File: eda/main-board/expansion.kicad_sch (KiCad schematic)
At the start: 15 parts, among them J2 Expansion, U11 74HCT245, U13 74HCT138, U17 74HCT541, U18 74HCT541, U20 74HCT541

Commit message: Did stuff
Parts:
- renumbered J2 to J7
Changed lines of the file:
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@@
 (kicad_sch
-	(version 20231120)
+	(version 20250114)
 	(generator "eeschema")
-	(generator_version "8.0")
+	(generator_version "9.0")
 	(paper "A4")
 	(junction
@@
 	(label "A2"
 		(at 73.66 50.8 0)
-		(fields_autoplaced yes)
 		(effects
 			(font
@@
 	(label "e{slash}~{IRQ}"
 		(at 120.65 138.43 0)
-		(fields_autoplaced yes)
 		(effects
 			(font
@@
 	(label "IoSelect4"
 		(at 146.05 76.2 0)
-		(fields_autoplaced yes)
 		(effects
 			(font
@@
 	(label "A3"
 		(at 73.66 53.34 0)
-		(fields_autoplaced yes)
 		(effects
 			(font
@@
 	(label "IoSelect5"
 		(at 146.05 78.74 0)
-		(fields_autoplaced yes)
 		(effects
 			(font
@@
 	(label "e{slash}~{IRQ}"
 		(at 200.66 93.98 0)
-		(fields_autoplaced yes)
 		(effects
 			(font
@@
 	(label "IoSelect2"
 		(at 101.6 163.83 0)
-		(fields_autoplaced yes)
 		(effects
 			(font
@@
 	(label "IoSelect1"
 		(at 101.6 161.29 0)
-		(fields_autoplaced yes)
 		(effects
 			(font
@@
 	(label "A15"
 		(at 72.39 118.11 0)
-		(fields_autoplaced yes)
 		(effects
 			(font
@@
 	(label "IoSelect6"
 		(at 146.05 81.28 0)
-		(fields_autoplaced yes)
 		(effects
 			(font
@@
 	(label "e{slash}~{NMI}"
 		(at 200.66 91.44 0)
-		(fields_autoplaced yes)
 		(effects
 			(font
@@
 	(label "A14"
 		(at 72.39 115.57 0)
-		(fields_autoplaced yes)
 		(effects
 			(font
@@
 	(label "IoSelect2"
 		(at 146.05 71.12 0)
-		(fields_autoplaced yes)
 		(effects
 			(font
@@
 	(label "IoSelect7"
 		(at 101.6 176.53 0)
-		(fields_autoplaced yes)
 		(effects
 			(font
@@
 	(label "D2"
 		(at 195.58 48.26 0)
-		(fields_autoplaced yes)
 		(effects
 			(font
@@
 	(label "A13"
 		(at 72.39 113.03 0)
-		(fields_autoplaced yes)
 		(effects
 			(font
@@
 	(label "A10"
 		(at 72.39 105.41 0)
-		(fields_autoplaced yes)
 		(effects
 			(font
@@
 	(label "A7"
 		(at 74.93 161.29 0)
-		(fields_autoplaced yes)
 		(effects
 			(font
@@
 	(label "A9"
 		(at 72.39 102.87 0)
-		(fields_autoplaced yes)
 		(effects
 			(font
@@
 	(label "D6"
 		(at 195.58 58.42 0)
-		(fields_autoplaced yes)
 		(effects
 			(font
@@
 	(label "D7"
 		(at 195.58 60.96 0)
-		(fields_autoplaced yes)
 		(effects
 			(font
@@
 	(label "D0"
 		(at 195.58 43.18 0)
-		(fields_autoplaced yes)
 		(effects
 			(font
@@
 	(label "IoSelect1"
 		(at 146.05 68.58 0)
-		(fields_autoplaced yes)
 		(effects
 			(font
@@
 	(label "IoSelect6"
 		(at 101.6 173.99 0)
-		(fields_autoplaced yes)
 		(effects
 			(font
@@
 	(label "IoSelect0"
 		(at 146.05 66.04 0)
-		(fields_autoplaced yes)
 		(effects
 			(font
@@
 	(label "IoSelect5"
 		(at 101.6 171.45 0)
-		(fields_autoplaced yes)
 		(effects
 			(font
@@
 	(label "IoSelect7"
 		(at 146.05 83.82 0)
-		(fields_autoplaced yes)
 		(effects
 			(font
@@
 	(label "A8"
 		(at 74.93 163.83 0)
-		(fields_autoplaced yes)
 		(effects
 			(font
@@
 	(label "IoSelect0"
 		(at 101.6 158.75 0)
-		(fields_autoplaced yes)
 		(effects
 			(font
@@
 	(label "A6"
 		(at 74.93 158.75 0)
-		(fields_autoplaced yes)
 		(effects
 			(font
@@
 	(label "A11"
 		(at 72.39 107.95 0)
-		(fields_autoplaced yes)
 		(effects
 			(font
@@
 	(label "e{slash}~{NMI}"
 		(at 120.65 135.89 0)
-		(fields_autoplaced yes)
 		(effects
 			(font
@@
 	(label "D1"
 		(at 195.58 45.72 0)
-		(fields_autoplaced yes)
 		(effects
 			(font
@@
 	(label "A5"
 		(at 73.66 58.42 0)
-		(fields_autoplaced yes)
 		(effects
 			(font
@@
 	(label "D4"
 		(at 195.58 53.34 0)
-		(fields_autoplaced yes)
 		(effects
 			(font
@@
 	(label "IoSelect3"
 		(at 101.6 166.37 0)
-		(fields_autoplaced yes)
 		(effects
 			(font
@@
 	(label "A8"
 		(at 72.39 100.33 0)
-		(fields_autoplaced yes)
 		(effects
 			(font
@@
 	(label "IoSelect4"
 		(at 101.6 168.91 0)
-		(fields_autoplaced yes)
 		(effects
 			(font
@@
 	(label "IoSelect3"
 		(at 146.05 73.66 0)
-		(fields_autoplaced yes)
 		(effects
 			(font
@@
 	(label "A1"
 		(at 73.66 48.26 0)
-		(fields_autoplaced yes)
 		(effects
 			(font
@@
 	(label "A0"
 		(at 73.66 45.72 0)
-		(fields_autoplaced yes)
 		(effects
 			(font
@@
 	(label "A4"
 		(at 73.66 55.88 0)
-		(fields_autoplaced yes)
 		(effects
 			(font
@@
 	(label "A6"
 		(at 73.66 60.96 0)
-		(fields_autoplaced yes)
 		(effects
 			(font
@@
 	(label "~{ExtRomCS}"
 		(at 146.05 99.06 0)
-		(fields_autoplaced yes)
 		(effects
 			(font
@@
 	(label "A7"
 		(at 73.66 63.5 0)
-		(fields_autoplaced yes)
 		(effects
 			(font
@@
 	(label "A12"
 		(at 72.39 110.49 0)
-		(fields_autoplaced yes)
 		(effects
 			(font
@@
 	(label "D5"
 		(at 195.58 55.88 0)
-		(fields_autoplaced yes)
 		(effects
 			(font
@@
 	(label "D3"
 		(at 195.58 50.8 0)
-		(fields_autoplaced yes)
 		(effects
 			(font
@@
 		(shape bidirectional)
 		(at 168.91 137.16 0)
-		(fields_autoplaced yes)
 		(effects
 			(font
@@
 		(shape input)
 		(at 66.04 176.53 180)
-		(fields_autoplaced yes)
 		(effects
 			(font
@@
 		(shape bidirectional)
 		(at 168.91 134.62 0)
-		(fields_autoplaced yes)
 		(effects
 			(font
@@
 		(shape input)
 		(at 52.07 33.02 180)
-		(fields_autoplaced yes)
 		(effects
 			(font
@@
 		(shape output)
 		(at 163.83 127 0)
-		(fields_autoplaced yes)
 		(effects
 			(font
@@
 		(shape input)
 		(at 151.13 88.9 0)
-		(fields_autoplaced yes)
 		(effects
 			(font
@@
 		(shape input)
 		(at 220.98 35.56 0)
-		(fields_autoplaced yes)
 		(effects
 			(font
@@
 		(shape input)
 		(at 64.77 153.67 180)
-		(fields_autoplaced yes)
 		(effects
 			(font
@@
 		(shape input)
 		(at 165.1 66.04 180)
-		(fields_autoplaced yes)
 		(effects
 			(font
@@
 		(shape input)
 		(at 130.81 129.54 180)
-		(fields_autoplaced yes)
 		(effects
 			(font
@@
 		(dnp no)
 		(fields_autoplaced yes)
-		(property "Reference" "J2"
+		(property "Reference" "J7"
 			(at 139.7 35.56 0)
 			(effects

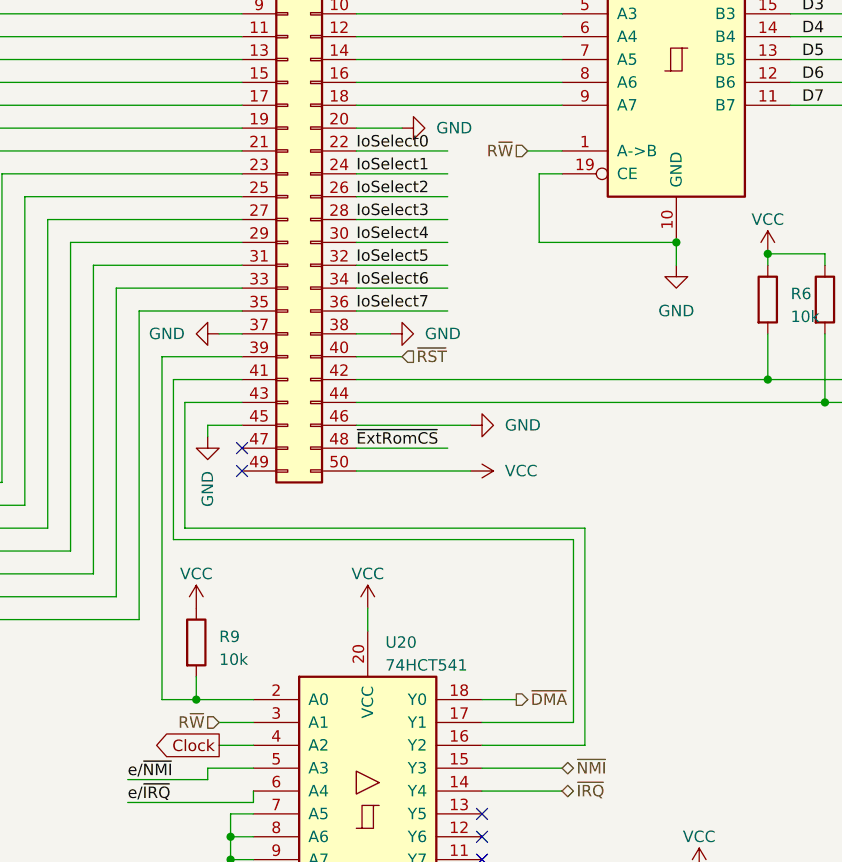
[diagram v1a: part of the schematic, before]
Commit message: fix: Traces straight over GND....
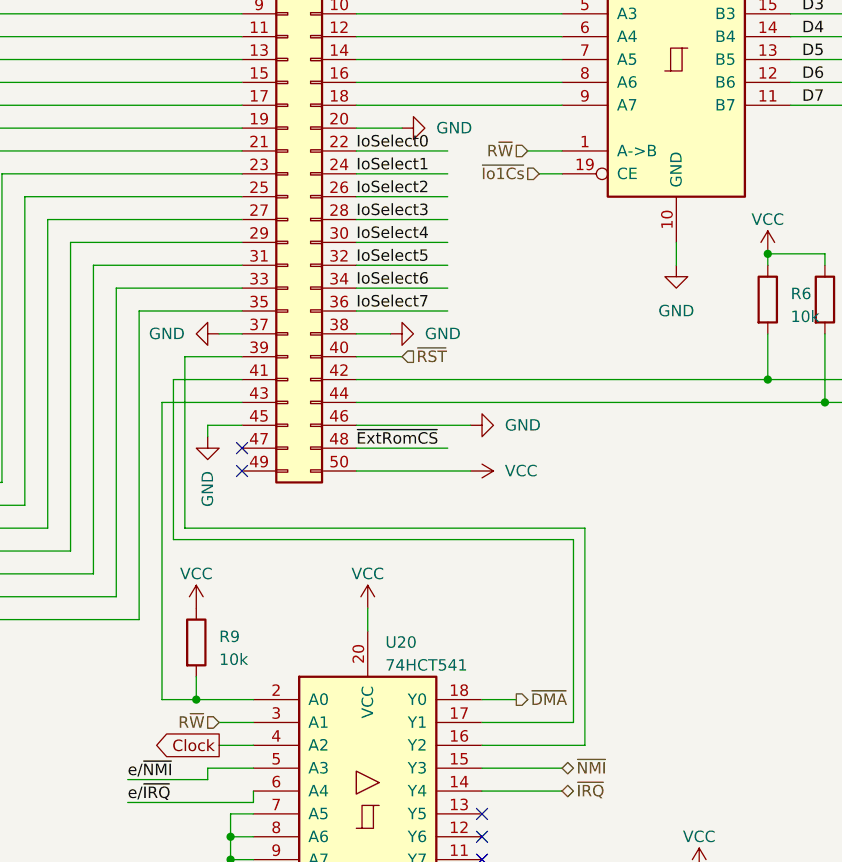
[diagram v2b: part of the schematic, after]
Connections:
- net GND: no longer U11.19 (CE)
- net ~{Io1Cs}: now also U11.19 (CE)
- net at R9.2, U20.2 (A0): now also J7.43 (Pin_43); no longer J7.39 (Pin_39)
- net at U20.16 (Y2): now also J7.39 (Pin_39); no longer J7.43 (Pin_43)
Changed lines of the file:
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@@
-	)
-	(junction
-		(at 181.61 76.2)
-		(diameter 0)
-		(color 0 0 0 0)
 	)
 	(junction
@@
 	(wire
 		(pts
+			(xy 124.46 93.98) (xy 133.35 93.98)
+		)
+		(stroke
+			(width 0)
+			(type default)
+		)
+	)
+	(wire
+		(pts
 			(xy 101.6 60.96) (xy 133.35 60.96)
 		)
@@
 	(wire
 		(pts
-			(xy 166.37 68.58) (xy 166.37 76.2)
-		)
-		(stroke
-			(width 0)
-			(type default)
-		)
-	)
-	(wire
-		(pts
 			(xy 111.76 73.66) (xy 111.76 107.95)
 		)
@@
 	(wire
 		(pts
-			(xy 127 107.95) (xy 127 93.98)
+			(xy 127 88.9) (xy 127 107.95)
 		)
 		(stroke
@@
 		)
 	)
-	(wire
-		(pts
-			(xy 127 93.98) (xy 133.35 93.98)
-		)
-		(stroke
-			(width 0)
-			(type default)
-		)
-	)
 	(bus
 		(pts
@@
 		)
 	)
+	(wire
+		(pts
+			(xy 127 88.9) (xy 133.35 88.9)
+		)
+		(stroke
+			(width 0)
+			(type default)
+		)
+	)
 	(bus
 		(pts
@@
 	(wire
 		(pts
-			(xy 166.37 76.2) (xy 181.61 76.2)
-		)
-		(stroke
-			(width 0)
-			(type default)
-		)
-	)
-	(wire
-		(pts
 			(xy 181.61 78.74) (xy 181.61 76.2)
 		)
@@
 	(wire
 		(pts
-			(xy 124.46 88.9) (xy 124.46 127)
+			(xy 124.46 93.98) (xy 124.46 127)
 		)
 		(stroke
@@
 		(pts
 			(xy 101.6 50.8) (xy 133.35 50.8)
-		)
-		(stroke
-			(width 0)
-			(type default)
-		)
-	)
-	(wire
-		(pts
-			(xy 124.46 88.9) (xy 133.35 88.9)
 		)
 		(stroke
@@
 		)
 	)
+	(hierarchical_label "~{Io1Cs}"
+		(shape input)
+		(at 166.37 68.58 180)
+		(effects
+			(font
+				(size 1.27 1.27)
+			)
+			(justify right)
+		)
+	)
